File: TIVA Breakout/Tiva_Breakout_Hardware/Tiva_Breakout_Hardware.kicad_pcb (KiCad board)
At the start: 2 copper layers, 141.4 x 70.3 mm, 67 parts, among them U1 TM4C129E_Launchpad

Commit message: fixed some silkscreen labels
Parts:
- renumbered 12V_A1 to 12V
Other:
- board text added: "PATCH PANEL"
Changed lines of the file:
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@@
   (page A4)
   (layers
-    (0 F.Cu signal hide)
-    (31 B.Cu signal hide)
+    (0 F.Cu signal)
+    (31 B.Cu signal)
     (32 B.Adhes user)
     (33 F.Adhes user)
@@
     (descr "Through hole straight pin header, 2x05, 1.27mm pitch, double rows")
     (tags "Through hole pin header THT 2x05 1.27mm double row")
-    (fp_text reference 12V_A1 (at 4.445 -2.159) (layer F.SilkS)
+    (fp_text reference 12V (at 4.445 -2.159) (layer F.SilkS)
       (effects (font (size 1 1) (thickness 0.15)))
     )
@@
     (effects (font (size 1 1.016) (thickness 0.15)) (justify left))
   )
-  (gr_text 30V_R (at 198.0692 86.233) (layer F.SilkS)
-    (effects (font (size 1 1.016) (thickness 0.15)) (justify left))
+  (gr_text "PATCH PANEL" (at 200.4822 86.233) (layer F.SilkS)
+    (effects (font (size 1 1.016) (thickness 0.15)))
   )
   (gr_line (start 157.0482 76.2) (end 157.0482 76.581) (layer F.SilkS) (width 0.12))

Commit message: completely finished PRR and BOM
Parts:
- 12V_A1: renamed from 12V; footprint Connector_PinHeader_1.27mm:PinHeader_2x05_P1.27mm_Vertical -> MRDT_Connectors:JTAG_ARM_Connector_10_Pin
- Conn30V_L1, Conn30V_R1, ConnPCH_C2: footprint Connector_PinHeader_1.27mm:PinHeader_2x05_P1.27mm_Vertical -> MRDT_Connectors:JTAG_ARM_Connector_10_Pin
- moved D12 1.91 mm to (214.7, 116.6)
- moved D13 1.91 mm to (217.9, 116.6)
- moved D14 1.91 mm to (221.1, 116.6)
- moved R12 1.91 mm to (214.7, 112.1)
- moved R13 1.91 mm to (217.9, 112.1)
- moved R14 1.91 mm to (221.1, 112.1)
- moved R22 1.27 mm to (195.0, 96.0)
- moved Conn30V_L1 1.27 mm to (103.6, 81.7)
- moved D15 1.27 mm to (202.6, 92.2)
- moved D16 1.27 mm to (205.8, 92.2)
- moved D17 1.27 mm to (209.0, 92.2)
- moved D18 1.27 mm to (212.2, 92.2)
- moved D21 1.27 mm to (198.2, 92.2)
- moved D22 1.27 mm to (195.0, 92.2)
- moved D23 1.27 mm to (191.8, 92.2)
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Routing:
- net PB6_EN: track 118.9 -> 100.5 mm
- net PB1_EN: track 106.4 -> 102.6 mm
- net LOG_EN: track 70.1 -> 72.0 mm
- net VOUT_EN: track 71.7 -> 73.6 mm
- net ACT_EN: track 70.8 -> 72.7 mm
- net PB4_EN: track 106.9 -> 108.8 mm
- net PB5_EN: track 97.5 -> 95.6 mm
- net GND: track 53.8 -> 55.4 mm, vias 27 -> 26
- net M3_EN: track 17.3 -> 18.6 mm
- net M2_ISENSE: track 16.3 -> 17.6 mm
- net M2_EN: track 16.3 -> 17.6 mm
- net M1_ISENSE: track 12.7 -> 14.0 mm
- net M4_EN: track 22.2 -> 23.5 mm
- net M1_EN: track 18.4 -> 19.7 mm
- net M3_ISENSE: track 19.2 -> 20.5 mm
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
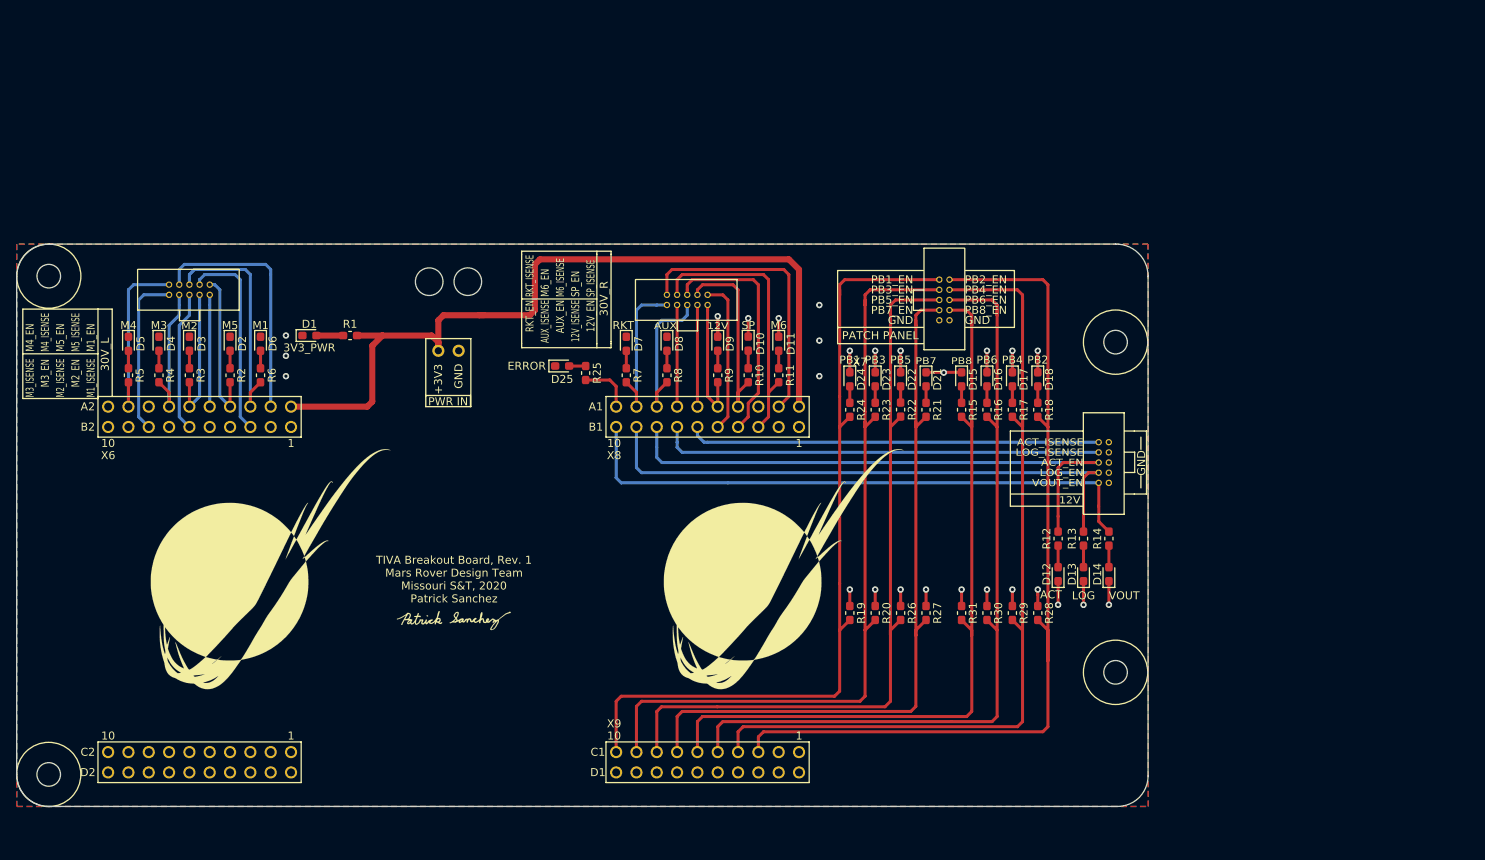
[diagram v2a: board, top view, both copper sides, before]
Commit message: 30V connectors and part of patch panel finished
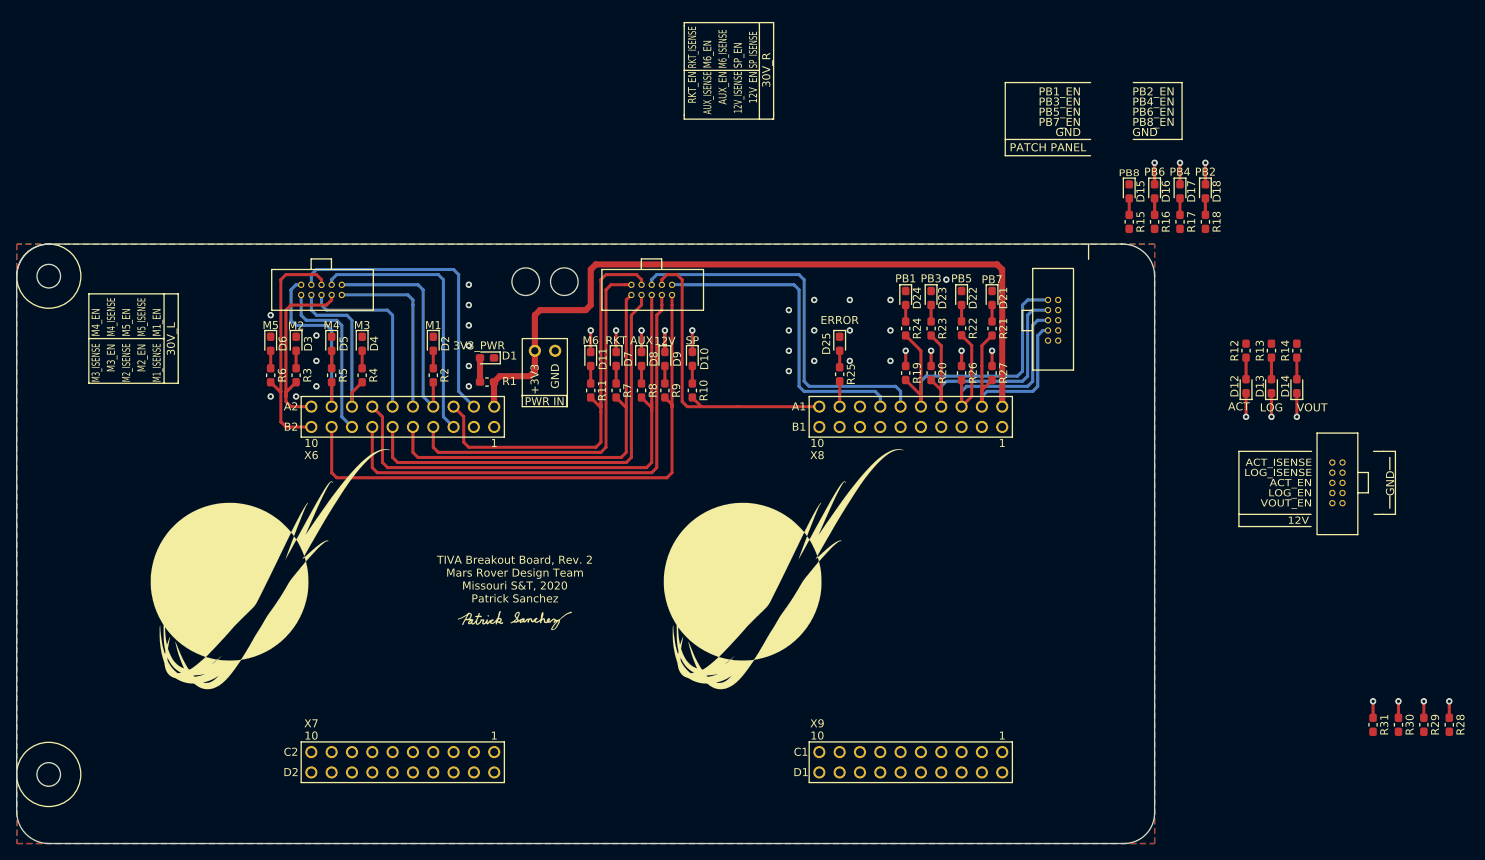
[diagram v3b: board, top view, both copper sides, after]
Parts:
- removed the REF** at (221.9, 128.8)
- removed the REF** at (221.9, 87.6)
- moved R28 53.3 mm to (263.6, 135.4)
- moved R29 53.3 mm to (260.4, 135.4)
- moved R31 53.3 mm to (254.1, 135.4)
- moved R30 53.3 mm to (257.3, 135.4)
- moved D25 34.8 mm to (187.4, 87.8), turned to 270 degrees
- moved D12 33.2 mm to (238.2, 93.1)
- moved D13 33.2 mm to (241.4, 93.1)
- moved D14 33.2 mm to (244.6, 93.1)
- moved R12 33.2 mm to (238.2, 88.6)
- moved R13 33.2 mm to (241.4, 88.6)
- moved R14 33.2 mm to (244.6, 88.6)
- moved R25 31.8 mm to (187.4, 91.6)
- moved D15 31.5 mm to (223.6, 68.7)
- moved D17 31.5 mm to (229.9, 68.7)
- moved R15 31.5 mm to (223.6, 72.5)
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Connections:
- Conn30V_L1 pad 1: M3_ISENSE -> M1_EN
- Conn30V_L1 pad 10: M1_EN -> M3_ISENSE
- Conn30V_L1 pad 2: M4_EN -> M1_ISENSE
- Conn30V_L1 pad 3: M3_EN -> M5_ISENSE
- Conn30V_L1 pad 4: M4_ISENSE -> M2_EN
- Conn30V_L1 pad 5: M2_ISENSE -> M5_EN
- Conn30V_L1 pad 6: M5_EN -> M2_ISENSE
- Conn30V_L1 pad 7: M2_EN -> M4_ISENSE
- Conn30V_L1 pad 8: M5_ISENSE -> M3_EN
- Conn30V_L1 pad 9: M1_ISENSE -> M4_EN
- Conn30V_R1 pad 1: RKT_EN -> SP_ISENSE
- Conn30V_R1 pad 10: SP_ISENSE -> RKT_EN
- Conn30V_R1 pad 2: RKT_ISENSE -> 12V_EN
- Conn30V_R1 pad 3: AUX_ISENSE -> SP_EN
- Conn30V_R1 pad 4: M6_EN -> 12V_ISENSE
- Conn30V_R1 pad 5: AUX_EN -> M6_ISENSE
- Conn30V_R1 pad 6: M6_ISENSE -> AUX_EN
- Conn30V_R1 pad 7: 12V_ISENSE -> M6_EN
- Conn30V_R1 pad 8: SP_EN -> AUX_ISENSE
- Conn30V_R1 pad 9: 12V_EN -> RKT_ISENSE
- U1 pad PA4: Net-(U1-PadPA4) -> 12V_EN
- U1 pad PA5: Net-(U1-PadPA5) -> M5_EN
- U1 pad PB2: RKT_EN -> ERROR
- U1 pad PB3: ERROR -> SP_EN
- U1 pad PB5: Net-(U1-PadPB5) -> RKT_ISENSE
- U1 pad PC4: Net-(U1-PadPC4) -> PB5_EN
- U1 pad PC5: SP_EN -> PB3_EN
- U1 pad PC6: 12V_EN -> PB1_EN
- U1 pad PC7: AUX_EN -> Net-(U1-PadPC7)
- U1 pad PD3: AUX_ISENSE -> SP_ISENSE
- U1 pad PD5: M2_EN -> M2_ISENSE
- U1 pad PE0: M6_EN -> Net-(U1-PadPE0)
- U1 pad PE1: M6_ISENSE -> Net-(U1-PadPE1)
- U1 pad PE2: SP_ISENSE -> Net-(U1-PadPE2)
- U1 pad PE4: RKT_ISENSE -> PB7_EN
- U1 pad PE5: 12V_ISENSE -> M6_ISENSE
- U1 pad PK0: Net-(U1-PadPK0) -> RKT_EN
- U1 pad PK1: M2_ISENSE -> AUX_ISENSE
- U1 pad PK2: Net-(U1-PadPK2) -> 12V_ISENSE
- U1 pad PL0: PB7_EN -> Net-(U1-PadPL0)
- U1 pad PL1: PB5_EN -> Net-(U1-PadPL1)
- U1 pad PL2: PB3_EN -> Net-(U1-PadPL2)
- U1 pad PL3: PB1_EN -> Net-(U1-PadPL3)
- U1 pad PN4: Net-(U1-PadPN4) -> M2_EN
- U1 pad PP0: M5_EN -> M6_EN
- U1 pad PP4: Net-(U1-PadPP4) -> M3_EN
- U1 pad PQ0: M3_EN -> AUX_EN
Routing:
- net PB2_EN: track 113.8 -> 0.00 mm
- net PB4_EN: track 108.8 -> 0.00 mm
- net PB6_EN: track 100.5 -> 0.00 mm
- net PB8_EN: track 96.7 -> 0.00 mm
- net VOUT_EN: track 73.6 -> 0.00 mm
- net ACT_EN: track 72.7 -> 0.00 mm
- net LOG_EN: track 72.0 -> 0.00 mm
- net PB7_EN: track 92.4 -> 31.2 mm
- net PB3_EN: track 99.4 -> 38.8 mm
- net PB1_EN: track 102.6 -> 42.5 mm
- net PB5_EN: track 95.6 -> 36.3 mm
- net 12V_EN: track 16.3 -> 72.5 mm
- net LOG_ISENSE: track 55.5 -> 0.00 mm
- net ACT_ISENSE: track 51.6 -> 0.00 mm
- net 12V_ISENSE: track 12.7 -> 63.0 mm
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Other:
- board size 141.4 x 70.3 mm -> 142.2 x 74.9 mm
- board text added: "TIVA Breakout Board, Rev. 2 Mars Rover Design Team Missouri S&T, 2020 Patrick Sanchez"
- board text removed: "TIVA Breakout Board, Rev. 1 Mars Rover Design Team Missouri S&T, 2020 Patrick Sanchez"
